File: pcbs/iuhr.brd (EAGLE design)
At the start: 38.4 x 23 mm, 72 parts, among them IC1 TPS77033, IC2 MEGA48/88/168-AU, Q1 20.000MHz

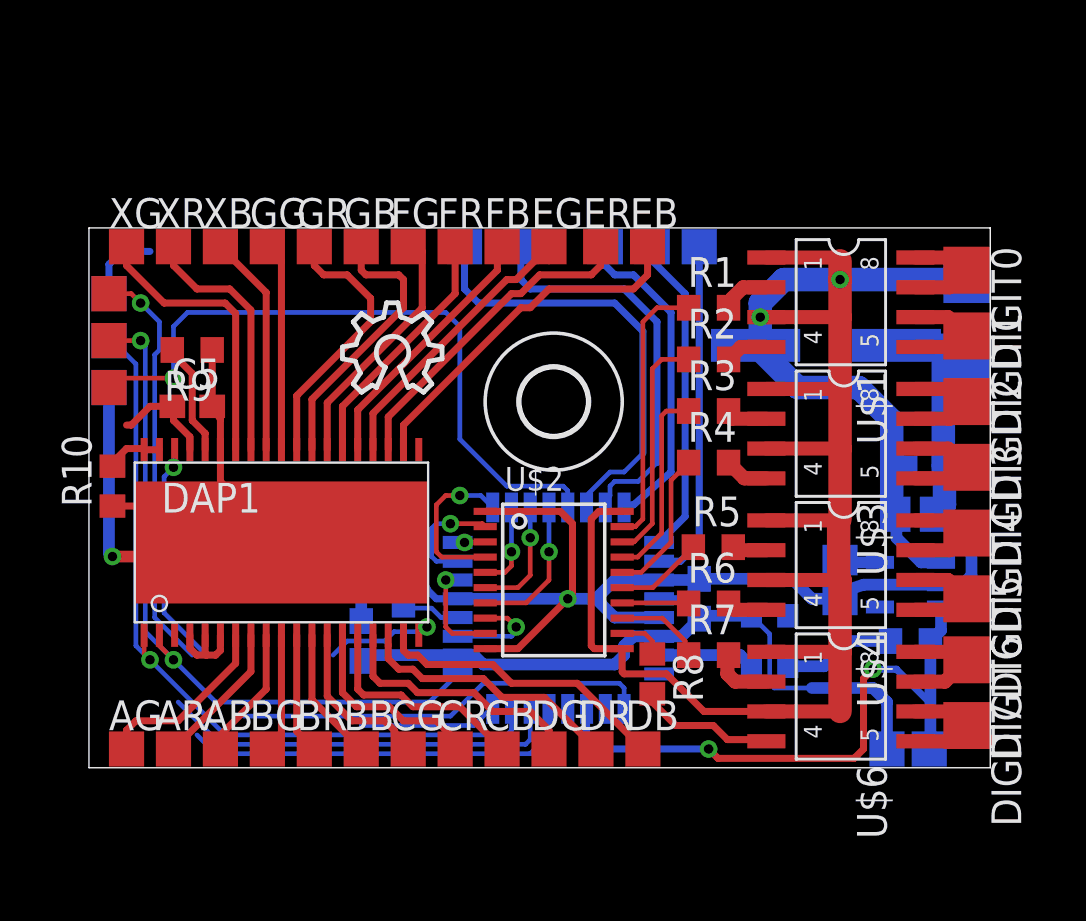
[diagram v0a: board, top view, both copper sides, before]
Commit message: No Airwires. No unapproved DRC Errors.
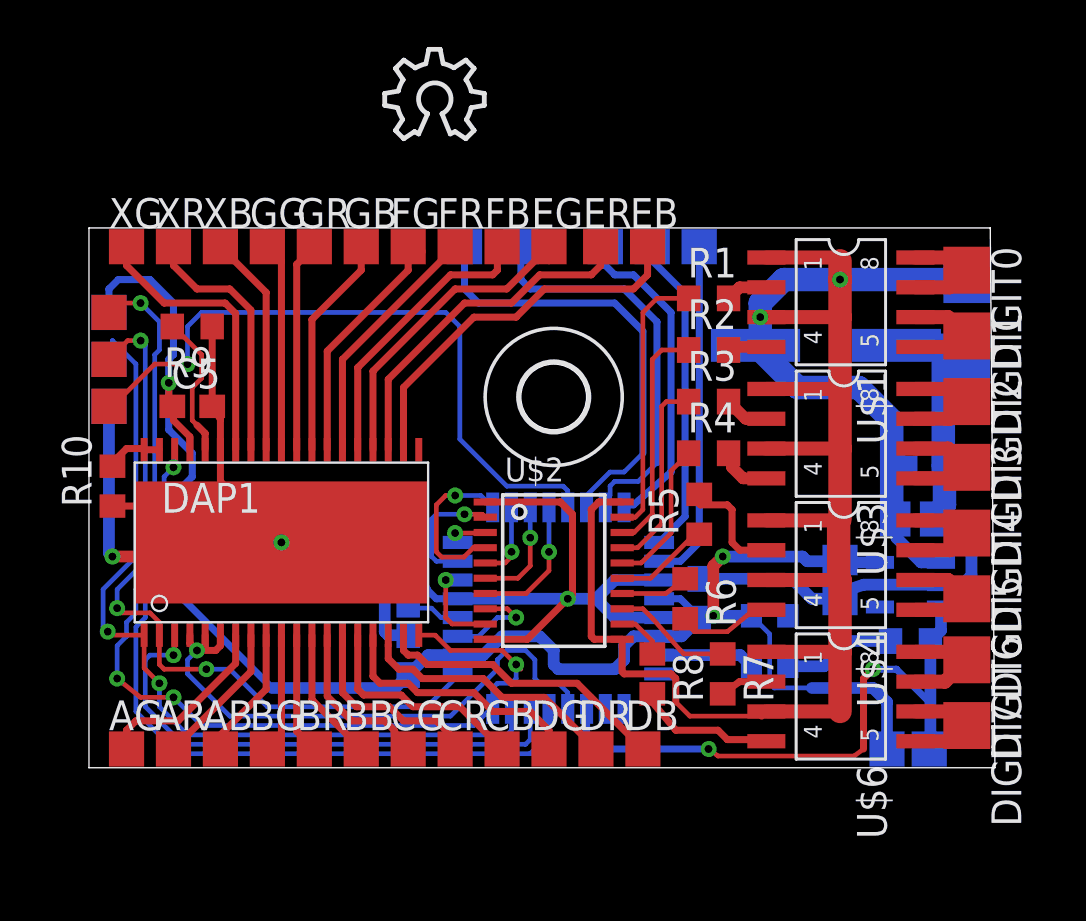
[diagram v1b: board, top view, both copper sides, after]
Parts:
- moved LOGO2 10.9 mm to (12.6, 26.8)
- moved C3 2.09 mm to (13.6, 4.80)
- moved R5 1.52 mm to (26.0, 10.8), turned to 90 degrees
- moved R6 1.02 mm to (25.4, 7.20), turned to 270 degrees
- moved R7 1.00 mm to (27.0, 4.00), turned to 270 degrees
- moved R9 1.00 mm to (4.40, 18.8)
- moved U$5 0.80 mm to (0.00, 17.4)
- moved R2 0.40 mm to (26.4, 17.8)
- moved R3 0.40 mm to (26.4, 15.6)
- moved R4 0.40 mm to (26.4, 13.4)
- moved U$2 0.40 mm to (19.8, 8.40)
- moved R1 0.40 mm to (26.4, 20.0)
- moved C4 0.20 mm to (35.2, 10.6)
- moved H2 0.20 mm to (19.8, 15.8)
- moved C1 0.20 mm to (13.6, 7.80)
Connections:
- net GSCK: now also IC2.12; no longer IC2.9
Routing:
- net VCC: track 40.0 -> 72.7 mm, vias 0 -> 3
- net MISO: track 28.5 -> 43.5 mm, vias 2 -> 4
- net GND: track 97.1 -> 104.1 mm, vias 2 -> 3
- net GSLAT: track 17.1 -> 22.6 mm, vias 0 -> 1
- net XBLINK: track 26.3 -> 31.7 mm
- net GSCK: track 21.3 -> 24.7 mm, vias 0 -> 1
- net N$43: track 1.63 -> 4.88 mm
- net N$23: track 11.5 -> 8.96 mm
- net MOSI: track 33.3 -> 35.7 mm, vias 1 -> 2
- net N$44: track 1.72 -> 4.11 mm
- net N$25: track 11.8 -> 9.52 mm
- net SCK: track 30.2 -> 32.2 mm, vias 2 -> 3
- net +12V: track 86.7 -> 88.1 mm
- net N$51: track 3.75 -> 5.14 mm
- net N$55: track 4.83 -> 6.19 mm
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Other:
- board size 38.4 x 23 mm -> 38.6 x 23 mm

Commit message: Add ground plane and thermal vias.
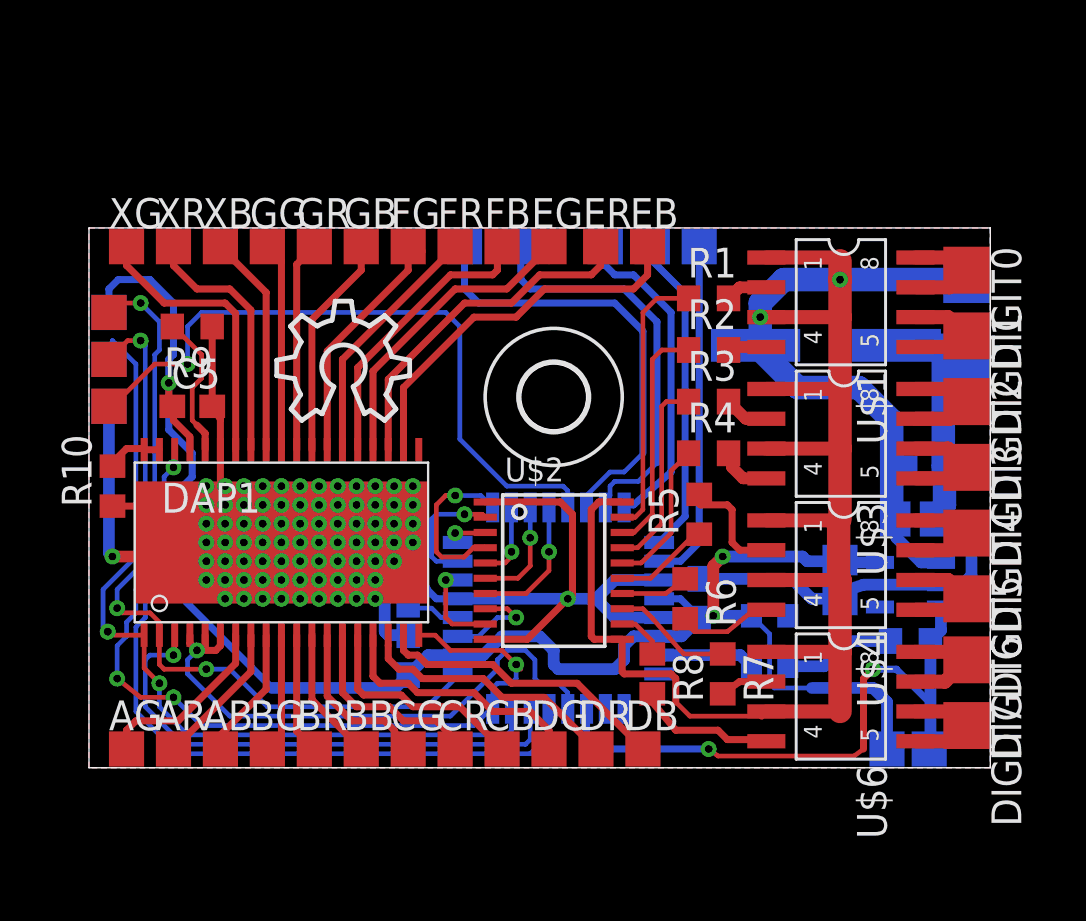
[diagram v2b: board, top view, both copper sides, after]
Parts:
- removed LOGO2: OSHW_LOGO_8MILX0150-NT, ea:OSHW_8X150_NOTEXT
- added LOGO1: OSHW_LOGO_8MILX0200-NT, ea:OSHW_8X200_NOTEXT
- added LOGO3: OSHW_LOGO_8MILX0350-NT, ea:OSHW_8X350_NOTEXT
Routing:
- net GND: vias 3 -> 80
- added copper zone on layer 1, net GND
- added copper zone on layer 16, net GND
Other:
- board size 38.6 x 23 mm -> 38.4 x 23 mm
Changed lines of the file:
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@@
 <layer number="14" name="Route14" color="1" fill="6" visible="no" active="no"/>
 <layer number="15" name="Route15" color="4" fill="6" visible="no" active="no"/>
-<layer number="16" name="Bottom" color="1" fill="1" visible="no" active="yes"/>
+<layer number="16" name="Bottom" color="1" fill="1" visible="yes" active="yes"/>
 <layer number="17" name="Pads" color="2" fill="1" visible="yes" active="yes"/>
 <layer number="18" name="Vias" color="2" fill="1" visible="yes" active="yes"/>
@@
 <layer number="20" name="Dimension" color="15" fill="1" visible="yes" active="yes"/>
 <layer number="21" name="tPlace" color="7" fill="1" visible="yes" active="yes"/>
-<layer number="22" name="bPlace" color="7" fill="1" visible="no" active="yes"/>
+<layer number="22" name="bPlace" color="7" fill="1" visible="yes" active="yes"/>
 <layer number="23" name="tOrigins" color="15" fill="1" visible="yes" active="yes"/>
-<layer number="24" name="bOrigins" color="15" fill="1" visible="no" active="yes"/>
+<layer number="24" name="bOrigins" color="15" fill="1" visible="yes" active="yes"/>
 <layer number="25" name="tNames" color="7" fill="1" visible="yes" active="yes"/>
-<layer number="26" name="bNames" color="7" fill="1" visible="no" active="yes"/>
+<layer number="26" name="bNames" color="7" fill="1" visible="yes" active="yes"/>
 <layer number="27" name="tValues" color="7" fill="1" visible="no" active="yes"/>
 <layer number="28" name="bValues" color="7" fill="1" visible="no" active="yes"/>
@@
 <layer number="38" name="bTest" color="7" fill="1" visible="no" active="yes"/>
 <layer number="39" name="tKeepout" color="4" fill="11" visible="yes" active="yes"/>
-<layer number="40" name="bKeepout" color="1" fill="11" visible="no" active="yes"/>
+<layer number="40" name="bKeepout" color="1" fill="11" visible="yes" active="yes"/>
 <layer number="41" name="tRestrict" color="4" fill="10" visible="no" active="yes"/>
 <layer number="42" name="bRestrict" color="1" fill="10" visible="no" active="yes"/>
@@
 <layer number="50" name="dxf" color="7" fill="1" visible="no" active="no"/>
 <layer number="51" name="tDocu" color="7" fill="1" visible="yes" active="yes"/>
-<layer number="52" name="bDocu" color="7" fill="1" visible="no" active="yes"/>
+<layer number="52" name="bDocu" color="7" fill="1" visible="yes" active="yes"/>
 <layer number="53" name="tGND_GNDA" color="7" fill="9" visible="no" active="no"/>
 <layer number="54" name="bGND_GNDA" color="1" fill="9" visible="no" active="no"/>
@@
 <board>
 <plain>
-<wire x1="0" y1="0" x2="38.6" y2="0" width="0" layer="20"/>
-<wire x1="38.6" y1="0" x2="38.4" y2="23" width="0" layer="20"/>
+<wire x1="0" y1="0" x2="38.4" y2="0" width="0" layer="20"/>
+<wire x1="38.4" y1="0" x2="38.4" y2="23" width="0" layer="20"/>
 <wire x1="38.4" y1="23" x2="0" y2="23" width="0" layer="20"/>
 <wire x1="0" y1="23" x2="0" y2="0" width="0" layer="20"/>
@@
 <element name="C5" library="resistor" package="C0603" value="100nF" x="4.4" y="15.4"/>
 <element name="H2" library="holes" package="2,8" value="MOUNT-HOLE2.8" x="19.8" y="15.8"/>
-<element name="LOGO2" library="ea" package="OSHW_8X150_NOTEXT" value="OSHW_LOGO_8MILX0150-NT" x="12.6" y="26.8"/>
+<element name="LOGO1" library="ea" package="OSHW_8X200_NOTEXT" value="OSHW_LOGO_8MILX0200-NT" x="8" y="14.8"/>
+<element name="LOGO3" library="ea" package="OSHW_8X350_NOTEXT" value="OSHW_LOGO_8MILX0350-NT" x="14.6" y="12.6" rot="MR0"/>
 </elements>
 <signals>
@@
 <wire x1="12.75" y1="5.65" x2="12.6" y2="5.8" width="0.5" layer="16"/>
 <wire x1="12.6" y1="5.8" x2="12.6" y2="8.6" width="0.5" layer="16"/>
+<polygon width="0.2" layer="1" isolate="0.3">
+<vertex x="0" y="23"/>
+<vertex x="38.4" y="23"/>
+<vertex x="38.4" y="0"/>
+<vertex x="0" y="0"/>
+</polygon>
+<polygon width="0.2" layer="16" isolate="0.3">
+<vertex x="0" y="23"/>
+<vertex x="38.4" y="23"/>
+<vertex x="38.4" y="0"/>
+<vertex x="0" y="0"/>
+</polygon>
+<via x="7.4" y="9.6" extent="1-16" drill="0.3302"/>
+<via x="6.6" y="9.6" extent="1-16" drill="0.3302"/>
+<via x="6.6" y="8.8" extent="1-16" drill="0.3302"/>
+<via x="7.4" y="8.8" extent="1-16" drill="0.3302"/>
+<via x="6.6" y="8" extent="1-16" drill="0.3302"/>
+<via x="7.4" y="8" extent="1-16" drill="0.3302"/>
+<via x="5.8" y="8" extent="1-16" drill="0.3302"/>
+<via x="5.8" y="8.8" extent="1-16" drill="0.3302"/>
+<via x="5.8" y="9.6" extent="1-16" drill="0.3302"/>
+<via x="5" y="9.6" extent="1-16" drill="0.3302"/>
+<via x="5" y="8.8" extent="1-16" drill="0.3302"/>
+<via x="5" y="8" extent="1-16" drill="0.3302"/>
+<via x="5.8" y="7.2" extent="1-16" drill="0.3302"/>
+<via x="6.6" y="7.2" extent="1-16" drill="0.3302"/>
+<via x="7.4" y="7.2" extent="1-16" drill="0.3302"/>
+<via x="5.8" y="12" extent="1-16" drill="0.3302"/>
+<via x="6.6" y="12" extent="1-16" drill="0.3302"/>
+<via x="5.8" y="11.2" extent="1-16" drill="0.3302"/>
+<via x="6.6" y="11.2" extent="1-16" drill="0.3302"/>
+<via x="5" y="11.2" extent="1-16" drill="0.3302"/>
+<via x="5" y="12" extent="1-16" drill="0.3302"/>
+<via x="5" y="10.4" extent="1-16" drill="0.3302"/>
+<via x="5.8" y="10.4" extent="1-16" drill="0.3302"/>
+<via x="6.6" y="10.4" extent="1-16" drill="0.3302"/>
+<via x="8.2" y="12" extent="1-16" drill="0.3302"/>
+<via x="9" y="12" extent="1-16" drill="0.3302"/>
+<via x="8.2" y="11.2" extent="1-16" drill="0.3302"/>
+<via x="9" y="11.2" extent="1-16" drill="0.3302"/>
+<via x="7.4" y="11.2" extent="1-16" drill="0.3302"/>
+<via x="7.4" y="12" extent="1-16" drill="0.3302"/>
+<via x="7.4" y="10.4" extent="1-16" drill="0.3302"/>
+<via x="8.2" y="10.4" extent="1-16" drill="0.3302"/>
+<via x="9" y="10.4" extent="1-16" drill="0.3302"/>
+<via x="9" y="9.6" extent="1-16" drill="0.3302"/>
+<via x="10.6" y="12" extent="1-16" drill="0.3302"/>
+<via x="11.4" y="12" extent="1-16" drill="0.3302"/>
+<via x="10.6" y="11.2" extent="1-16" drill="0.3302"/>
+<via x="11.4" y="11.2" extent="1-16" drill="0.3302"/>
+<via x="9.8" y="11.2" extent="1-16" drill="0.3302"/>
+<via x="9.8" y="12" extent="1-16" drill="0.3302"/>
+<via x="9.8" y="10.4" extent="1-16" drill="0.3302"/>
+<via x="10.6" y="10.4" extent="1-16" drill="0.3302"/>
+<via x="11.4" y="10.4" extent="1-16" drill="0.3302"/>
+<via x="9.8" y="9.6" extent="1-16" drill="0.3302"/>
+<via x="10.6" y="9.6" extent="1-16" drill="0.3302"/>
+<via x="11.4" y="9.6" extent="1-16" drill="0.3302"/>
+<via x="13" y="12" extent="1-16" drill="0.3302"/>
+<via x="13.8" y="12" extent="1-16" drill="0.3302"/>
+<via x="13" y="11.2" extent="1-16" drill="0.3302"/>
+<via x="13.8" y="11.2" extent="1-16" drill="0.3302"/>
+<via x="12.2" y="11.2" extent="1-16" drill="0.3302"/>
+<via x="12.2" y="12" extent="1-16" drill="0.3302"/>
+<via x="12.2" y="10.4" extent="1-16" drill="0.3302"/>
+<via x="13" y="10.4" extent="1-16" drill="0.3302"/>
+<via x="13.8" y="10.4" extent="1-16" drill="0.3302"/>
+<via x="12.2" y="9.6" extent="1-16" drill="0.3302"/>
+<via x="13" y="9.6" extent="1-16" drill="0.3302"/>
+<via x="13" y="8.8" extent="1-16" drill="0.3302"/>
+<via x="13.8" y="9.6" extent="1-16" drill="0.3302"/>
+<via x="9" y="8.8" extent="1-16" drill="0.3302"/>
+<via x="9.8" y="8.8" extent="1-16" drill="0.3302"/>
+<via x="9" y="8" extent="1-16" drill="0.3302"/>
+<via x="9.8" y="8" extent="1-16" drill="0.3302"/>
+<via x="8.2" y="8" extent="1-16" drill="0.3302"/>
+<via x="8.2" y="8.8" extent="1-16" drill="0.3302"/>
+<via x="8.2" y="7.2" extent="1-16" drill="0.3302"/>
+<via x="9" y="7.2" extent="1-16" drill="0.3302"/>
+<via x="9.8" y="7.2" extent="1-16" drill="0.3302"/>
+<via x="11.4" y="8.8" extent="1-16" drill="0.3302"/>
+<via x="12.2" y="8.8" extent="1-16" drill="0.3302"/>
+<via x="11.4" y="8" extent="1-16" drill="0.3302"/>
+<via x="12.2" y="8" extent="1-16" drill="0.3302"/>
+<via x="10.6" y="8" extent="1-16" drill="0.3302"/>
+<via x="10.6" y="8.8" extent="1-16" drill="0.3302"/>
+<via x="10.6" y="7.2" extent="1-16" drill="0.3302"/>
+<via x="11.4" y="7.2" extent="1-16" drill="0.3302"/>
+<via x="12.2" y="7.2" extent="1-16" drill="0.3302"/>
 </signal>
 <signal name="VCC">

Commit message: Improved Silkscreen.
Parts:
- removed LOGO3: OSHW_LOGO_8MILX0350-NT, ea:OSHW_8X350_NOTEXT
- moved LOGO1 2.15 mm to (10.0, 14.0)
- renumbered DAP1 to TLC5951, IC2 to ATMEGA88PA, U$1 to IRF7104, U$2 to ADG3123
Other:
- board text added: "(C) eKiwi 2013"
- board text added: "+12V"
- board text added: "0"
- board text added: "7"
- board text added: "A"
- board text added: "B"
- board text added: "BTN"
- board text added: "C"
- board text added: "D"
- board text added: "E"
- board text added: "Ei"
- board text added: "Encoder"
- board text added: "F"
- board text added: "G"
- board text added: "G R B"
- board text added: "GND"
- board text added: "ISP"
- board text added: "Licence: CERN OHL v1.2"
- board text added: "ON Button"
- board text added: "UART"
- board text added: "https://github.com/ekiwi/iuhr"

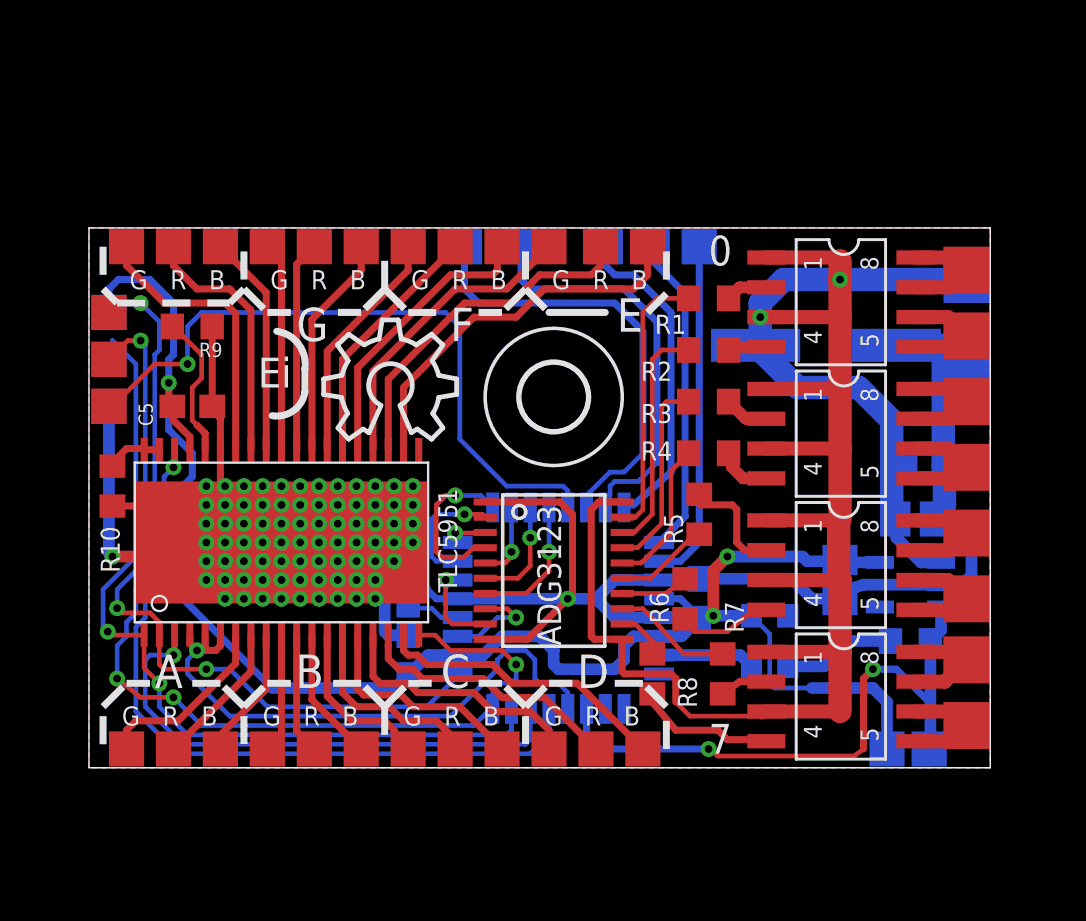
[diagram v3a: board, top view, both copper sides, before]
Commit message: Break out unused pins
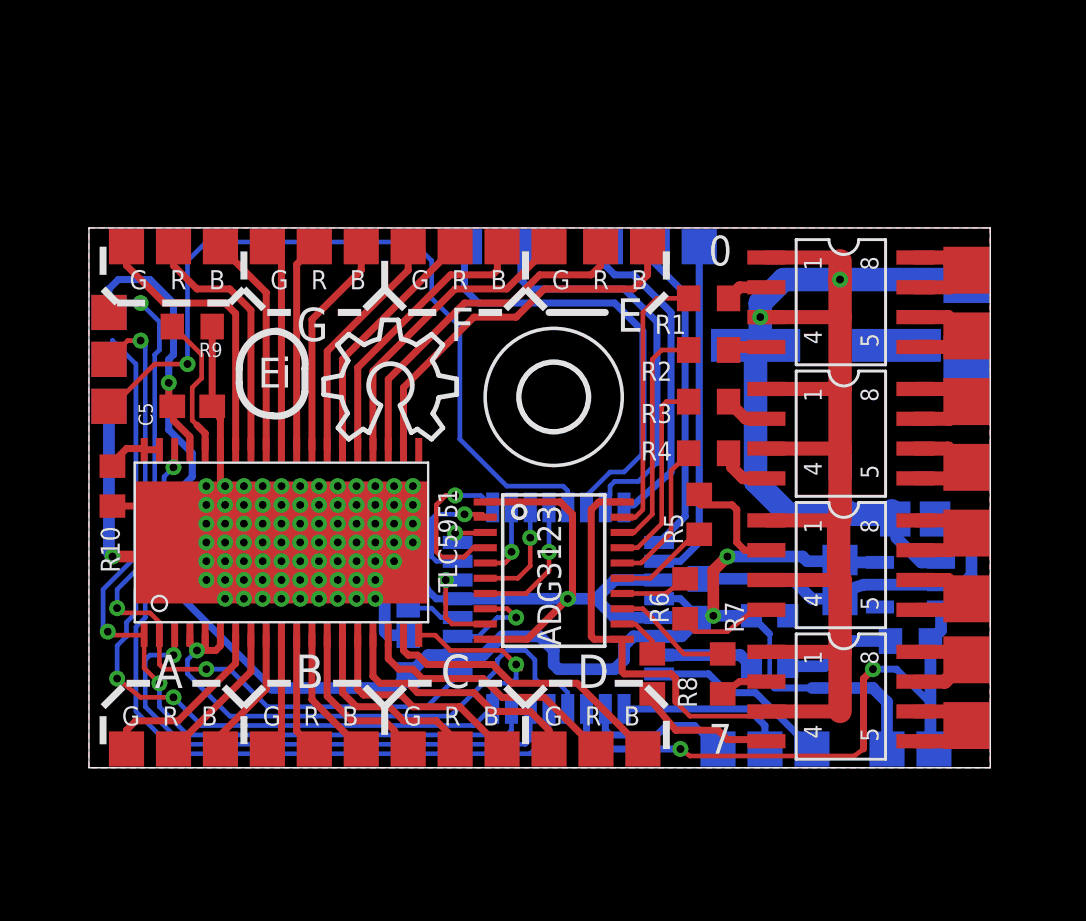
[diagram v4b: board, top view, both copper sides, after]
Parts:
- added PB7, PD5, PD6: TPTP15SQ, testpad:TP15SQ
- moved C11 3.69 mm to (32.0, 12.0), turned to 90 degrees
- moved ONBTN 0.20 mm to (36.0, 0.80)
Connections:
- new net N$56: ATMEGA88PA.9, PD5.TP
- new net N$57: ATMEGA88PA.10, PD6.TP
- new net N$58: ATMEGA88PA.8, PB7.TP
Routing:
- net GND: track 104.1 -> 93.2 mm
- net N$58: track 0.00 -> 7.83 mm
- net N$56: track 0.00 -> 7.29 mm
- net N$57: track 0.00 -> 6.37 mm
- net RESET: track 29.6 -> 34.6 mm
- net +12V: track 88.1 -> 89.5 mm
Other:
- board text added: "ON"
- board text removed: "ON Button"
